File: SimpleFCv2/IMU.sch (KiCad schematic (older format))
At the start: 17 parts, among them U2 MS5611, U3 MAG3110, U4 ICM-20689

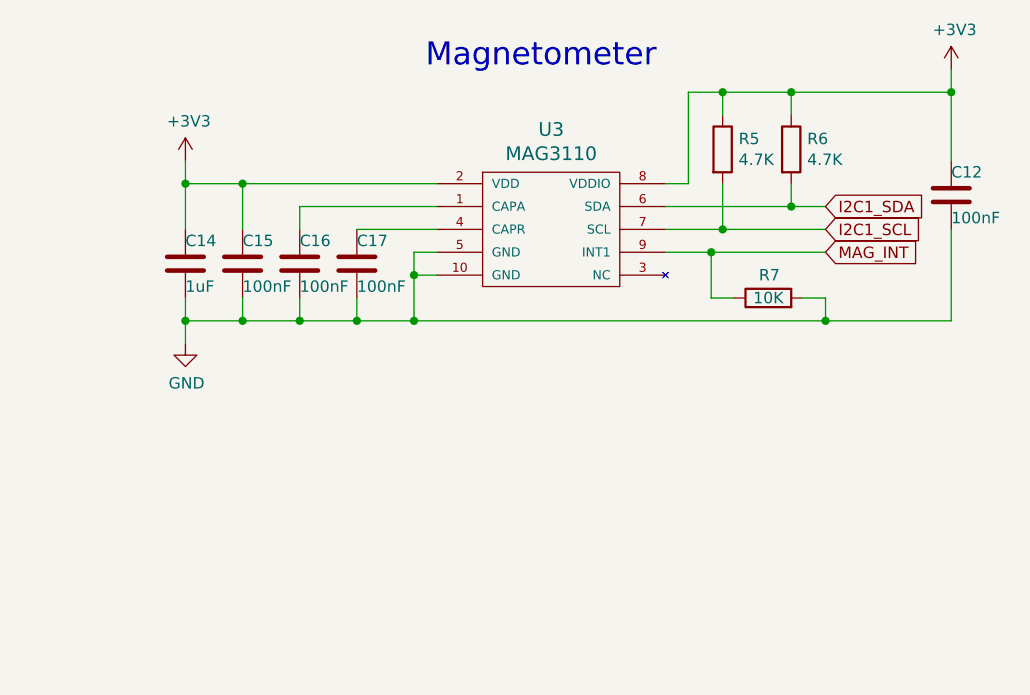
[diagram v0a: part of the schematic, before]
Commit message: Replace MAG3110 with MMC5883MA in SimpleFC
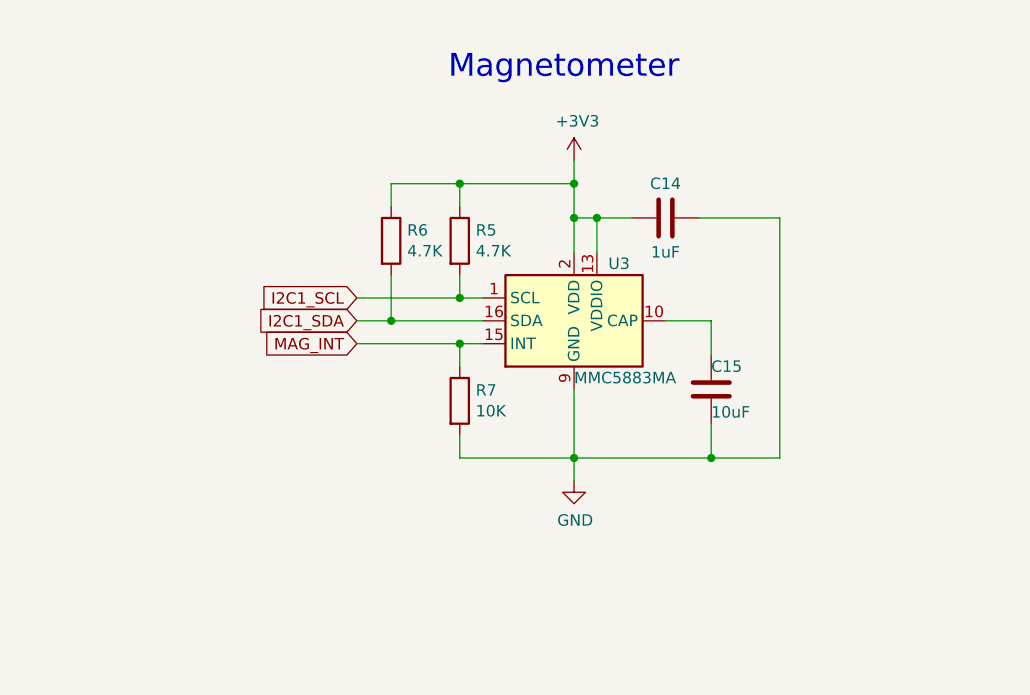
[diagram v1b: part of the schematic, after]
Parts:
- removed C12, C16, C17: 100nF, Capacitor_SMD:C_0603_1608Metric_Pad1.05x0.95mm_HandSolder, symbol Device:C
- removed U3: MAG3110, MEMS:DFN-10, symbol mems:MAG3110
- added U3: MMC5883MA, Package_LGA:LGA-16_3x3mm_P0.5mm, symbol Sensor_Magnetic:MMC5883MA
- C15: value 100nF -> 10uF
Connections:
- net +3V3: now also U3.13 (VDDIO), U3.2 (VDD); no longer C15.1
- net GND: now also U3.11 (GND), U3.9 (GND)
- net I2C1_SCL: now also U3.1 (SCL)
- net I2C1_SDA: now also U3.16 (SDA)
- net MAG_INT: now also U3.15 (INT)
- new net: C15.1, U3.10 (CAP)
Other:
- moved on the sheet: C14, C15, R5, R6
